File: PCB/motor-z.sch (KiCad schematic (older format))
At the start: 28 parts

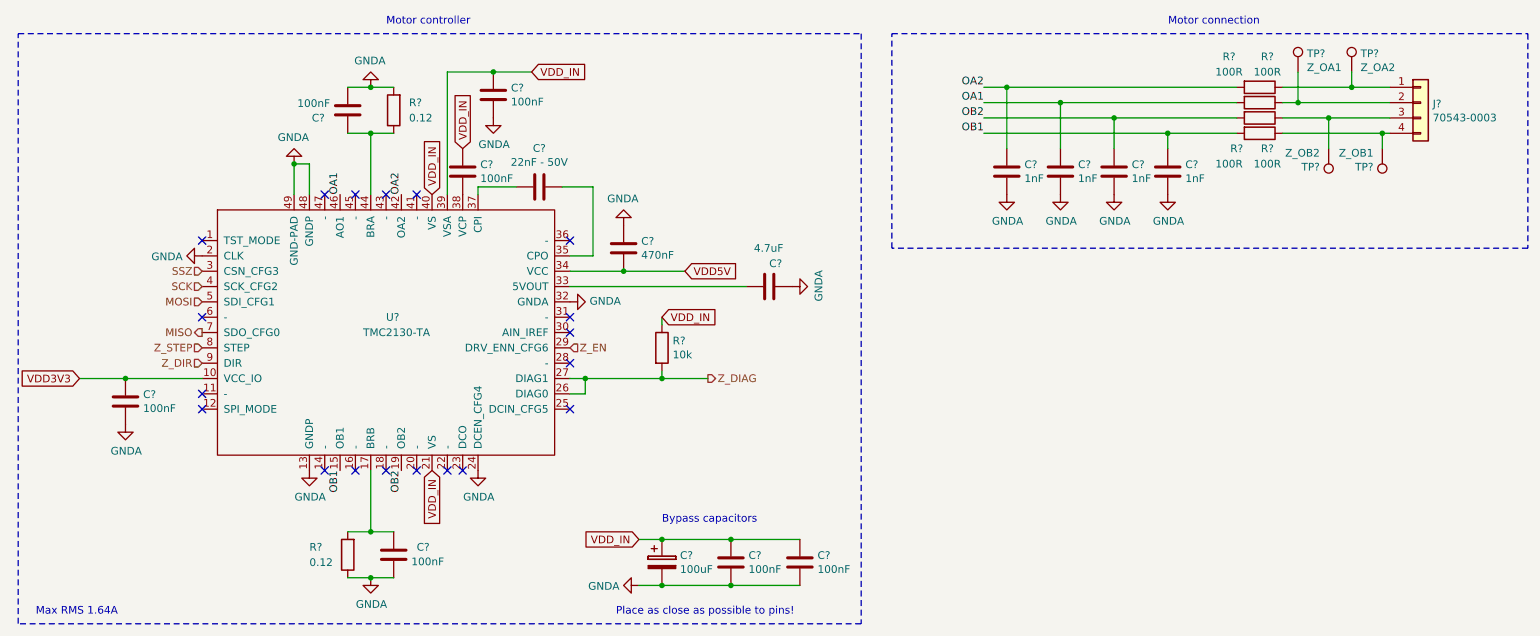
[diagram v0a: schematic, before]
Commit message: Fixed bugs found with ERC.
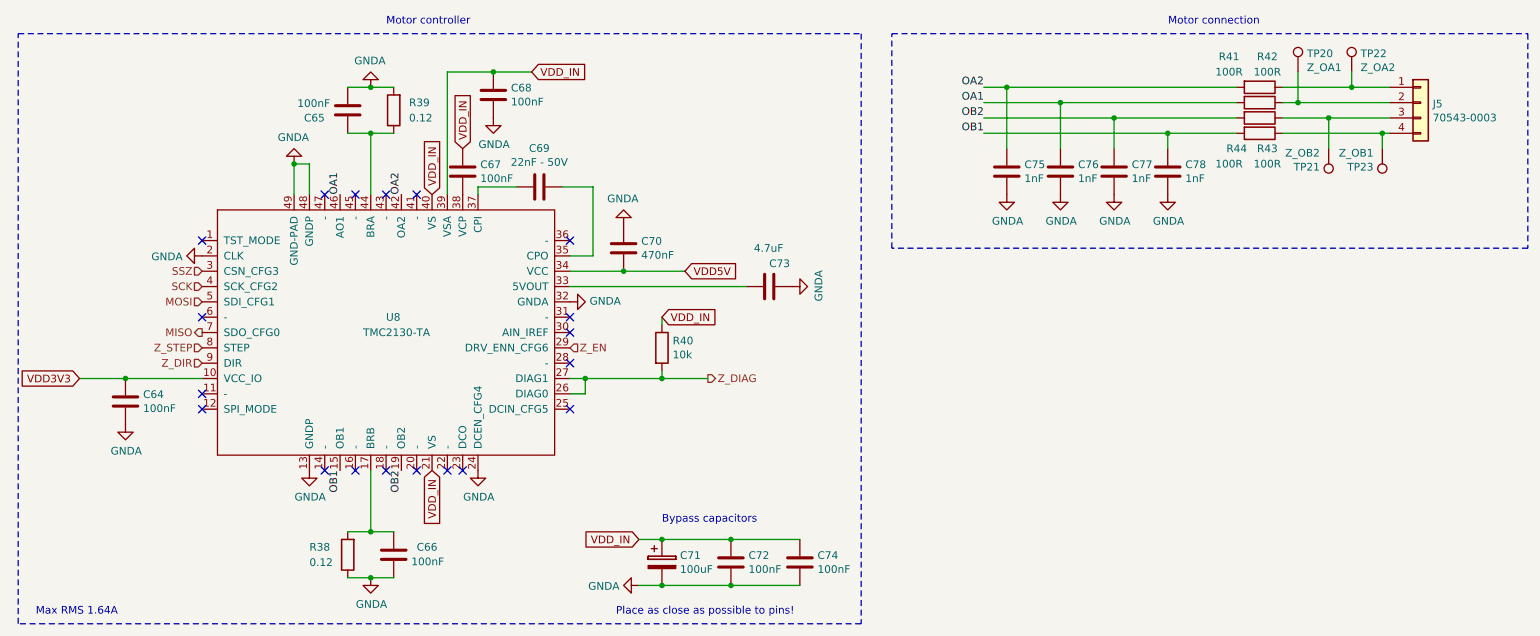
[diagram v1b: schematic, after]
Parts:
- removed C? (x5): 100nF, Capacitor_SMD:C_0603_1608Metric, symbol Device:C
- removed C?: 470nF, Capacitor_SMD:C_0603_1608Metric, symbol Device:C
- removed C?: 4.7uF, Resistor_SMD:R_0603_1608Metric, symbol Device:C
- removed C? (x3): 1nF, Resistor_SMD:R_0603_1608Metric, symbol Device:C
- removed C?: 100uF, Capacitor_THT:CP_Radial_D6.3mm_P2.50mm, symbol Device:CP
- removed J?: 70543-0003, Connector_PinHeader_2.54mm:PinHeader_1x04_P2.54mm_Vertical, symbol Connector_Generic:Conn_01x04
- removed R? (x2): 0.12, Resistor_SMD:R_1206_3216Metric, symbol Device:R
- removed R?: 10k, Resistor_SMD:R_0603_1608Metric, symbol Device:R
- removed R? (x2): 100R, Resistor_SMD:R_0603_1608Metric, symbol Device:R
- removed TP?: Z_OA2, TestPoint:TestPoint_Pad_D1.0mm, symbol Connector_Specialized:Test_Point
- removed U?: TMC2130-TA, custom-footprints:TQFP-48-1EP_7x7mm_P0.5mm_EP4.8x4.8mm-Heatsink, symbol remram-custom:TMC2130-TA
- added C64, C65, C68, C72, C74: 100nF, Capacitor_SMD:C_0603_1608Metric, symbol Device:C
- added C70: 470nF, Capacitor_SMD:C_0603_1608Metric, symbol Device:C
- added C71: 100uF, Capacitor_THT:CP_Radial_D6.3mm_P2.50mm, symbol Device:CP
- added C73: 4.7uF, Resistor_SMD:R_0603_1608Metric, symbol Device:C
- added C75, C76, C78: 1nF, Resistor_SMD:R_0603_1608Metric, symbol Device:C
- added J5: 70543-0003, Connector_PinHeader_2.54mm:PinHeader_1x04_P2.54mm_Vertical, symbol Connector_Generic:Conn_01x04
- added R38, R39: 0.12, Resistor_SMD:R_1206_3216Metric, symbol Device:R
- added R40: 10k, Resistor_SMD:R_0603_1608Metric, symbol Device:R
- added R42, R44: 100R, Resistor_SMD:R_0603_1608Metric, symbol Device:R
- added TP22: Z_OA2, TestPoint:TestPoint_Pad_D1.0mm, symbol Connector_Specialized:Test_Point
- added U8: TMC2130-TA, custom-footprints:TQFP-48-1EP_7x7mm_P0.5mm_EP4.8x4.8mm-Heatsink, symbol remram-custom:TMC2130-TA
- gave numbers to parts that had none: 9
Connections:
- net GNDA: now also C64.2, C65.2, C68.2, C70.2, C71.2, C72.2, C73.2, C74.2, C75.2, C76.2, C78.2, R38.1, R39.2, U8.13 (GNDP), U8.2 (CLK), U8.24 (DCEN_CFG4), U8.32 (GNDA), U8.48 (GNDP), U8.49 (GND-PAD)
- net MISO: now also U8.7 (SDO_CFG0)
- net MOSI: now also U8.5 (SDI_CFG1)
- net OA1: now also C76.1, R42.2, U8.46 (AO1)
- net OA2: now also C75.1, U8.42 (OA2)
- net OB1: now also C78.1, R44.2, U8.15 (OB1)
- net OB2: now also U8.19 (OB2)
- net SCK: now also U8.4 (SCK_CFG2)
- net SSZ: now also U8.3 (CSN_CFG3)
- net VDD3V3: now also C64.1, U8.10 (VCC_IO)
- net VDD5V: now also C70.1, U8.34 (VCC)
- net VDD_IN: now also C68.1, C71.1, C72.1, C74.1, R40.1, U8.21 (VS), U8.39 (VSA), U8.40 (VS)
- net Z_DIAG: now also R40.2, U8.26 (DIAG0), U8.27 (DIAG1)
- net Z_DIR: now also U8.9 (DIR)
- net Z_EN: now also U8.29 (DRV_ENN_CFG6)
- net Z_STEP: now also U8.8 (STEP)
- net at C66.1: now also R38.2, U8.17 (BRB)
- net at C69.1: now also U8.35 (CPO)
- net at C69.2: now also U8.37 (CPI)
- net at C67.2: now also U8.38 (VCP)
- net at R41.1: now also J5.1 (Pin_1), TP22.1
- net at TP20.1: now also J5.2 (Pin_2), R42.1
- net at R43.1, TP21.1: now also J5.3 (Pin_3)
- net at TP23.1: now also J5.4 (Pin_4), R44.1
- new net: C65.1, R39.1, U8.44 (BRA)
- new net: C73.1, U8.33 (5VOUT)

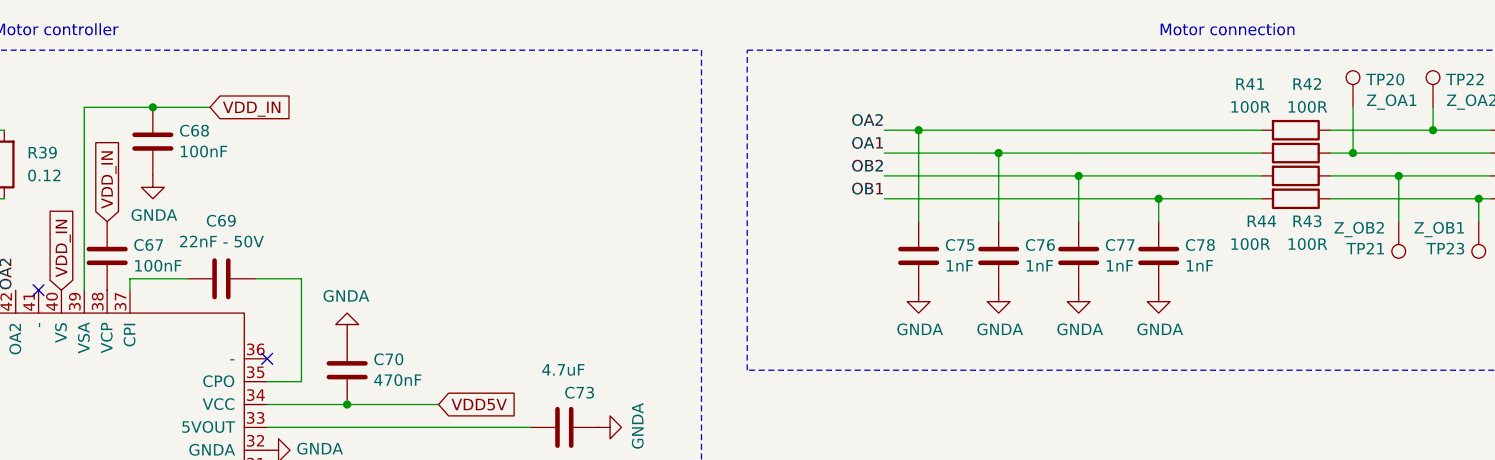
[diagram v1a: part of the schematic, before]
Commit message: Fixed annotations and assignment errors.
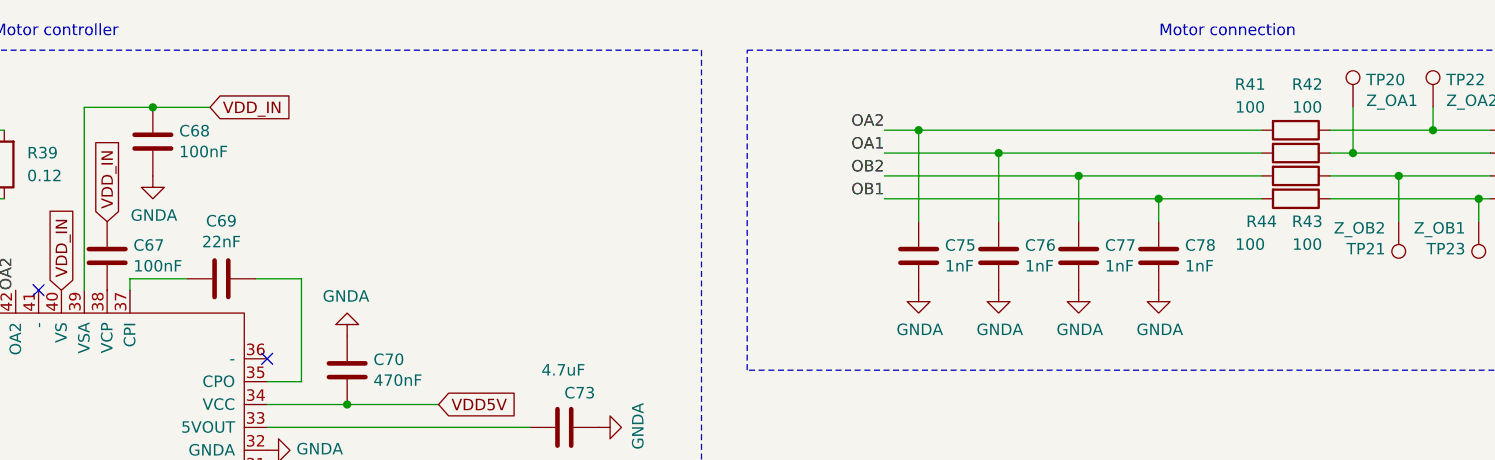
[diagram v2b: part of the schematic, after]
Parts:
- C69: value 22nF - 50V -> 22nF
- C73, C75, C76, C77, C78: footprint Resistor_SMD:R_0603_1608Metric -> Capacitor_SMD:C_0603_1608Metric
- R41, R42, R43, R44: value 100R -> 100
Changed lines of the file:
@@
 $Descr A4 11693 8268
 encoding utf-8
-Sheet 8 9
+Sheet 7 9
 Title "Motor Z-Axis"
 Date ""
@@
 $Comp
 L power:GNDA #PWR087
-U 1 1 5B03A4B5
+U 1 1 5AF8CE9E
 P 2450 3550
 F 0 "#PWR087" H 2450 3300 50  0001 C CNN
@@
 $Comp
 L Device:C C67
-U 1 1 5B03B9DC
+U 1 1 5AF8CEA0
 P 3450 1600
 F 0 "C67" H 3565 1646 50  0000 L CNN
@@
 $Comp
 L Device:C C69
-U 1 1 5B03BA1D
+U 1 1 5AF8CEA2
 P 3950 1700
 F 0 "C69" V 3698 1700 50  0000 C CNN
-F 1 "22nF - 50V" V 3789 1700 50  0000 C CNN
+F 1 "22nF" V 3789 1700 50  0000 C CNN
 F 2 "Capacitor_SMD:C_0603_1608Metric" H 3988 1550 50  0001 C CNN
 F 3 "~" H 3950 1700 50  0001 C CNN
@@
 F 0 "C73" V 5600 2350 50  0000 R CNN
 F 1 "4.7uF" V 5700 2450 50  0000 R CNN
-F 2 "Resistor_SMD:R_0603_1608Metric" H 5488 2200 50  0001 C CNN
+F 2 "Capacitor_SMD:C_0603_1608Metric" H 5488 2200 50  0001 C CNN
 F 3 "~" H 5450 2350 50  0001 C CNN
 	1    5450 2350
@@
 $Comp
 L Device:C C66
-U 1 1 5B047334
+U 1 1 5AF8CEB2
 P 3000 4100
 F 0 "C66" H 3150 4150 50  0000 L CNN
@@
 $Comp
 L Connector_Specialized:Test_Point TP21
-U 1 1 5B09FBC2
+U 1 1 5AF8CEBA
 P 9100 1450
 F 0 "TP21" H 9158 1570 50  0000 L CNN
@@
 $Comp
 L Connector_Specialized:Test_Point TP23
-U 1 1 5B09FBC9
+U 1 1 5AF8CEBB
 P 9450 1450
 F 0 "TP23" H 9508 1570 50  0000 L CNN
@@
 P 8650 1350
 F 0 "R44" V 8750 1200 50  0000 C CNN
-F 1 "100R" V 8850 1150 50  0000 C CNN
+F 1 "100" V 8850 1150 50  0000 C CNN
 F 2 "Resistor_SMD:R_0603_1608Metric" V 8580 1350 50  0001 C CNN
 F 3 "~" H 8650 1350 50  0001 C CNN
@@
 F 0 "C78" H 8165 1646 50  0000 L CNN
 F 1 "1nF" H 8165 1555 50  0000 L CNN
-F 2 "Resistor_SMD:R_0603_1608Metric" H 8088 1450 50  0001 C CNN
+F 2 "Capacitor_SMD:C_0603_1608Metric" H 8088 1450 50  0001 C CNN
 F 3 "~" H 8050 1600 50  0001 C CNN
 	1    8050 1600
@@
 F 0 "C77" H 7815 1646 50  0000 L CNN
 F 1 "1nF" H 7815 1555 50  0000 L CNN
-F 2 "Resistor_SMD:R_0603_1608Metric" H 7738 1450 50  0001 C CNN
+F 2 "Capacitor_SMD:C_0603_1608Metric" H 7738 1450 50  0001 C CNN
 F 3 "~" H 7700 1600 50  0001 C CNN
 	1    7700 1600
@@
 F 0 "C76" H 7465 1646 50  0000 L CNN
 F 1 "1nF" H 7465 1555 50  0000 L CNN
-F 2 "Resistor_SMD:R_0603_1608Metric" H 7388 1450 50  0001 C CNN
+F 2 "Capacitor_SMD:C_0603_1608Metric" H 7388 1450 50  0001 C CNN
 F 3 "~" H 7350 1600 50  0001 C CNN
 	1    7350 1600
@@
 F 0 "C75" H 7115 1646 50  0000 L CNN
 F 1 "1nF" H 7115 1555 50  0000 L CNN
-F 2 "Resistor_SMD:R_0603_1608Metric" H 7038 1450 50  0001 C CNN
+F 2 "Capacitor_SMD:C_0603_1608Metric" H 7038 1450 50  0001 C CNN
 F 3 "~" H 7000 1600 50  0001 C CNN
 	1    7000 1600
@@
 F 1 "100uF" H 4868 4105 50  0000 L CNN
 F 2 "Capacitor_THT:CP_Radial_D6.3mm_P2.50mm" H 4788 4000 50  0001 C CNN
-F 3 "https://www.mouser.de/ProductDetail/Wurth-Electronics/860010573007?qs=sGAEpiMZZMvwFf0viD3Y3aZipiehufnXDo3pM9Qdgp1gvK74JBMa%252bg%3d%3d" H 4750 4150 50  0001 C CNN
+F 3 "https://eu.mouser.com/datasheet/2/293/e-uvz-1219460.pdf" H 4750 4150 50  0001 C CNN
 	1    4750 4150
 	1    0    0    -1
@@
 $Comp
 L Device:R R43
-U 1 1 5B0A98C8
+U 1 1 5AF8CEC2
 P 8650 1250
 F 0 "R43" V 8850 1300 50  0000 C CNN
-F 1 "100R" V 8950 1300 50  0000 C CNN
+F 1 "100" V 8950 1300 50  0000 C CNN
 F 2 "Resistor_SMD:R_0603_1608Metric" V 8580 1250 50  0001 C CNN
 F 3 "~" H 8650 1250 50  0001 C CNN
@@
 P 8650 1150
 F 0 "R42" V 8350 1200 50  0000 C CNN
-F 1 "100R" V 8450 1200 50  0000 C CNN
+F 1 "100" V 8450 1200 50  0000 C CNN
 F 2 "Resistor_SMD:R_0603_1608Metric" V 8580 1150 50  0001 C CNN
 F 3 "~" H 8650 1150 50  0001 C CNN
@@
 $Comp
 L Device:R R41
-U 1 1 5B0A8ED9
+U 1 1 5AF8CEC0
 P 8650 1050
 F 0 "R41" V 8450 850 50  0000 C CNN
-F 1 "100R" V 8550 850 50  0000 C CNN
+F 1 "100" V 8550 850 50  0000 C CNN
 F 2 "Resistor_SMD:R_0603_1608Metric" V 8580 1050 50  0001 C CNN
 F 3 "~" H 8650 1050 50  0001 C CNN

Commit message: Saving work in progress.
Every component now has a 3D mode.
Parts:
- J5: footprint Connector_PinHeader_2.54mm:PinHeader_1x04_P2.54mm_Vertical -> custom-footprints:70543-0003
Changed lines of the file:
@@
 F 0 "J5" H 9779 1142 50  0000 L CNN
 F 1 "70543-0003" H 9779 1051 50  0000 L CNN
-F 2 "Connector_PinHeader_2.54mm:PinHeader_1x04_P2.54mm_Vertical" H 9700 1150 50  0001 C CNN
+F 2 "custom-footprints:70543-0003" H 9700 1150 50  0001 C CNN
 F 3 "https://www.mouser.de/ProductDetail/Molex/70543-0003?qs=sGAEpiMZZMs%252bGHln7q6pm%252bS0pk2Wo0XxCD3CKlCQrmU%3d" H 9700 1150 50  0001 C CNN
 	1    9700 1150

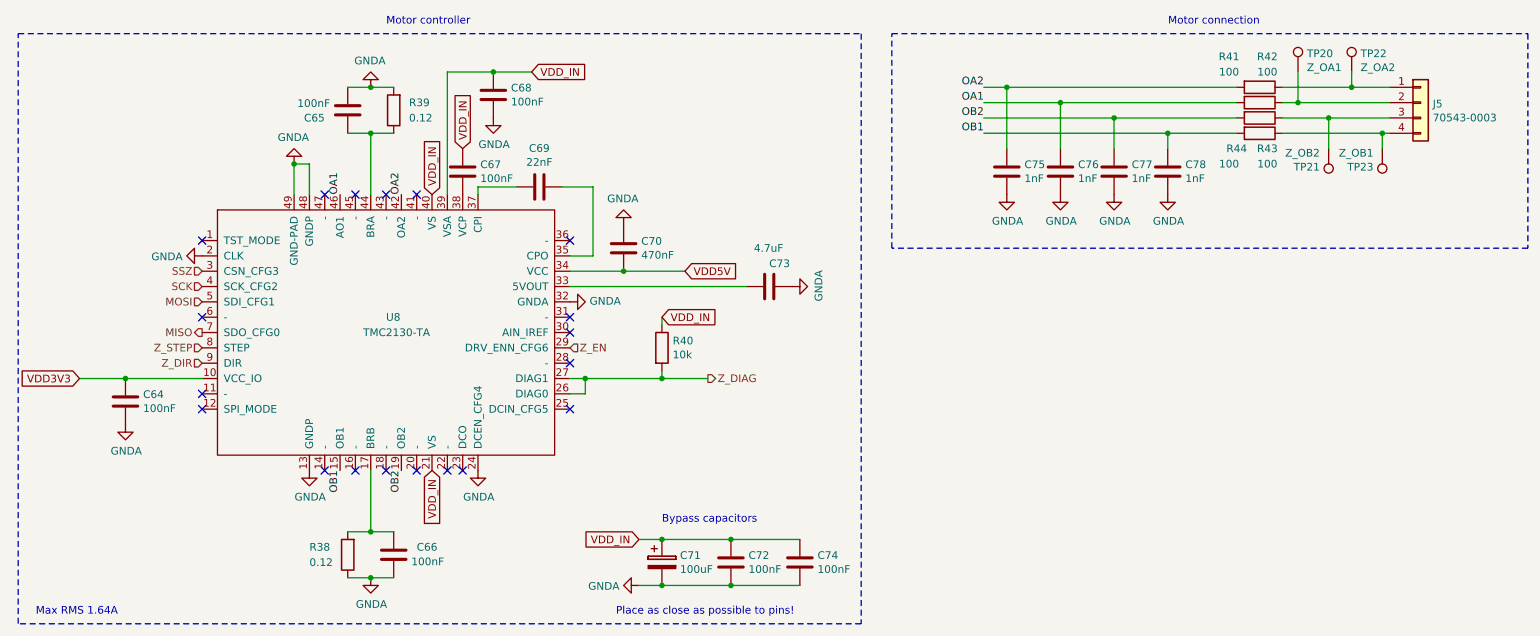
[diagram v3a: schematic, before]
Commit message: Removed logic level converter. Changed LDO.
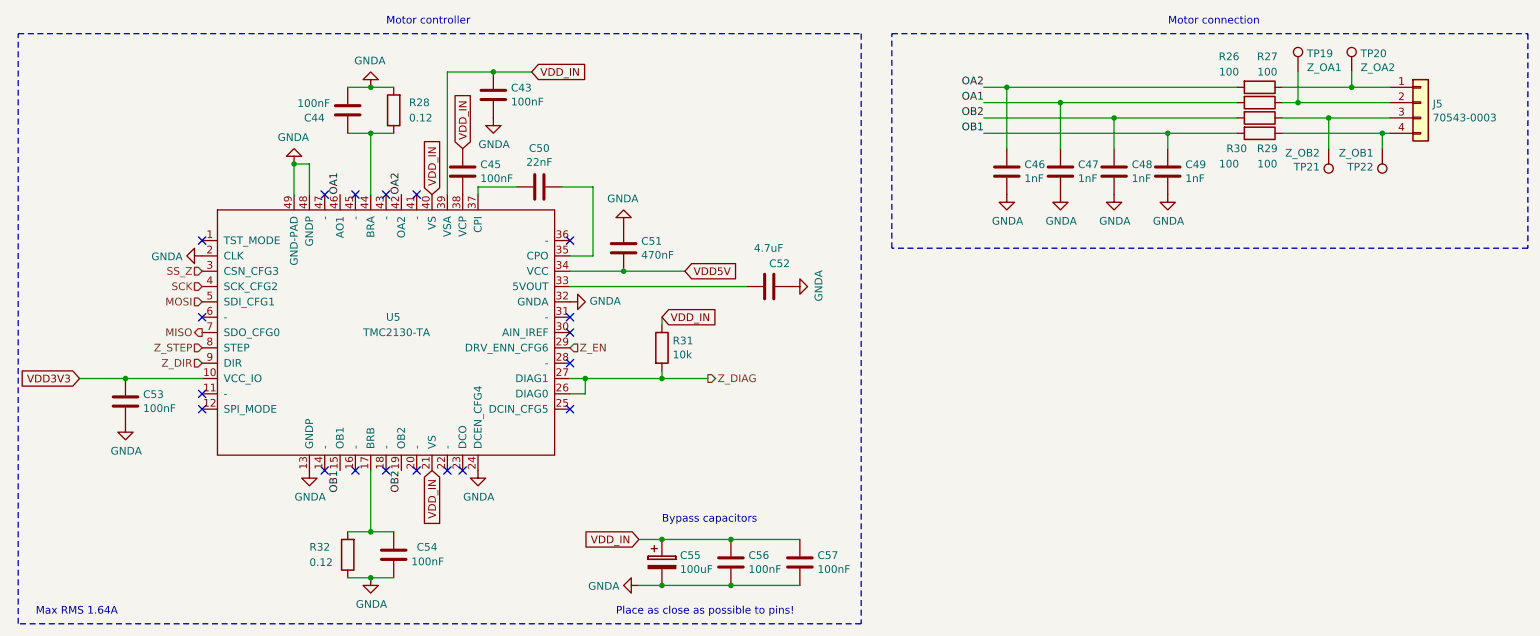
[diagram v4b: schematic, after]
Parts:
- renumbered C68 to C43, C65 to C44, C67 to C45, C75 to C46, C76 to C47, C77 to C48, C78 to C49, C69 to C50, C70 to C51, C73 to C52, C64 to C53, C66 to C54, C71 to C55, C72 to C56, C74 to C57, R41 to R26, R42 to R27, R39 to R28, R43 to R29, R44 to R30, R40 to R31, R38 to R32, TP20 to TP19, TP22 to TP20, TP23 to TP22, U8 to U5
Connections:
- net SSZ renamed SS_Z
